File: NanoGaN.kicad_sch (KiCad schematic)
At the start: 9 parts, among them J1 U_DC, J2 GND, J3 Phase_U, J4 Phase_V, J5 Phase_W

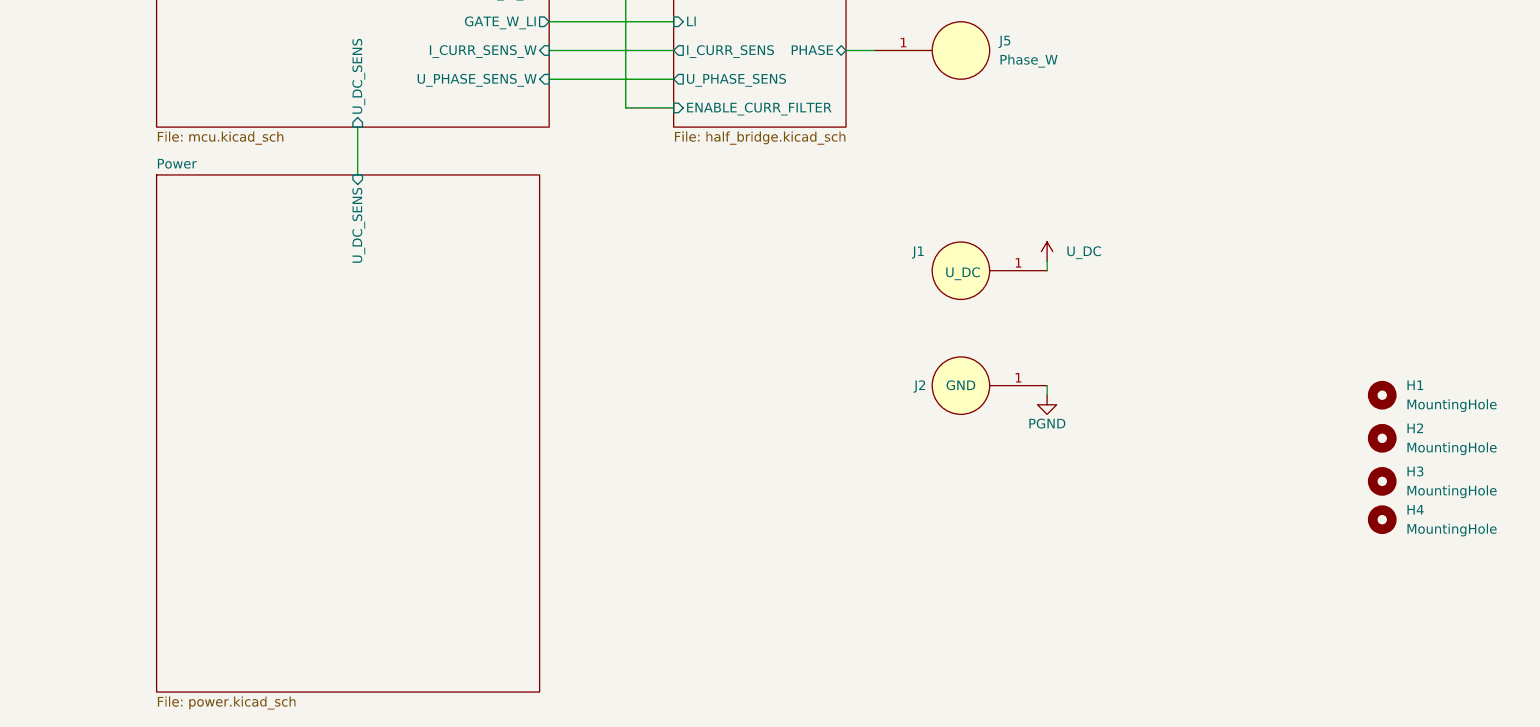
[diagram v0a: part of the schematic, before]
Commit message: Analog current filters were removed, some footprints were fixed and initial rough layout has been made.
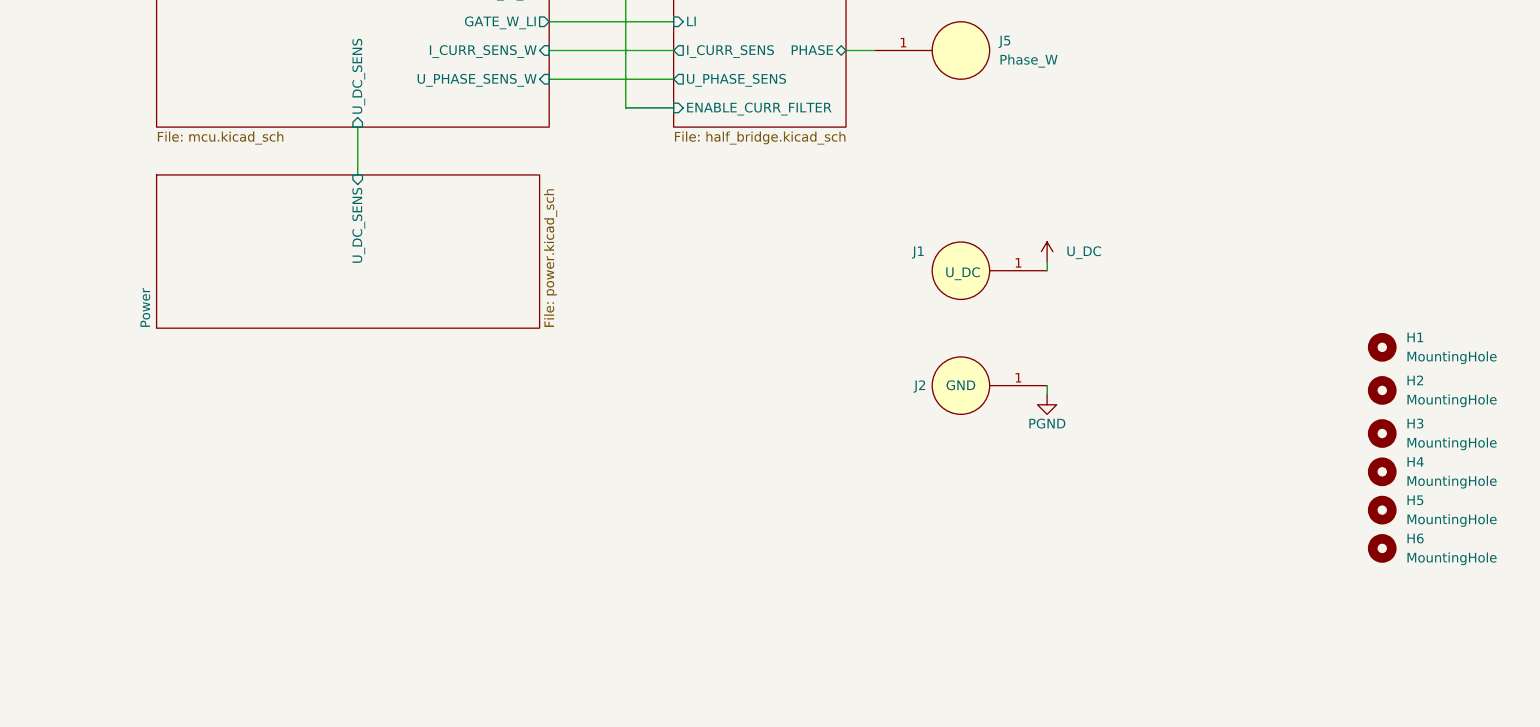
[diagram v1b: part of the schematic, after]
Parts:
- added H5, H6: MountingHole, MountingHole:MountingHole_3.2mm_M3, symbol Mechanical:MountingHole
- J1, J2, J3, J4, J5: footprint Connector:Power_Welding_Pad_10x10mm -> TerminalBlock_Wuerth:Wuerth_REDCUBE-THR_WP-THRBU_74650073_THR
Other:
- moved on the sheet: H1, H2, H3, H4
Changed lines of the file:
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@@
 			)
 		)
-		(property "Footprint" "Connector:Power_Welding_Pad_10x10mm"
+		(property "Footprint" "TerminalBlock_Wuerth:Wuerth_REDCUBE-THR_WP-THRBU_74650073_THR"
 			(at 205.74 93.98 0)
 			(effects
@@
 	)
 	(symbol
+		(lib_id "Mechanical:MountingHole")
+		(at 261.62 160.02 0)
+		(unit 1)
+		(exclude_from_sim no)
+		(in_bom yes)
+		(on_board yes)
+		(dnp no)
+		(fields_autoplaced yes)
+		(property "Reference" "H6"
+			(at 264.795 158.75 0)
+			(effects
+				(font
+					(size 1.27 1.27)
+				)
+				(justify left)
+			)
+		)
+		(property "Value" "MountingHole"
+			(at 264.795 161.29 0)
+			(effects
+				(font
+					(size 1.27 1.27)
+				)
+				(justify left)
+			)
+		)
+		(property "Footprint" "MountingHole:MountingHole_3.2mm_M3"
+			(at 261.62 160.02 0)
+			(effects
+				(font
+					(size 1.27 1.27)
+				)
+				(hide yes)
+			)
+		)
+		(property "Datasheet" "~"
+			(at 261.62 160.02 0)
+			(effects
+				(font
+					(size 1.27 1.27)
+				)
+				(hide yes)
+			)
+		)
+		(property "Description" ""
+			(at 261.62 160.02 0)
+			(effects
+				(font
+					(size 1.27 1.27)
+				)
+			)
+		)
+		(instances
+			(project "NanoGaN"
+				(path "/aa8a494f-605e-4a00-9d3c-daec94709fcb"
+					(reference "H6")
+					(unit 1)
+				)
+			)
+		)
+	)
+	(symbol
 		(lib_id "power:GND")
 		(at 217.17 139.7 0)
@@
 			)
 		)
-		(property "Footprint" "Connector:Power_Welding_Pad_10x10mm"
+		(property "Footprint" "TerminalBlock_Wuerth:Wuerth_REDCUBE-THR_WP-THRBU_74650073_THR"
 			(at 205.74 68.58 0)
 			(effects
@@
 			)
 		)
-		(property "Footprint" "Connector:Power_Welding_Pad_10x10mm"
+		(property "Footprint" "TerminalBlock_Wuerth:Wuerth_REDCUBE-THR_WP-THRBU_74650073_THR"
 			(at 205.74 123.19 0)
 			(effects
@@
 	(symbol
 		(lib_id "Mechanical:MountingHole")
-		(at 261.62 156.21 0)
+		(at 261.62 149.86 0)
 		(unit 1)
 		(exclude_from_sim no)
@@
 		(fields_autoplaced yes)
 		(property "Reference" "H4"
-			(at 264.795 154.94 0)
+			(at 264.795 148.59 0)
 			(effects
 				(font
@@
 		)
 		(property "Value" "MountingHole"
-			(at 264.795 157.48 0)
+			(at 264.795 151.13 0)
 			(effects
 				(font
@@
 		)
 		(property "Footprint" "MountingHole:MountingHole_3.2mm_M3"
-			(at 261.62 156.21 0)
+			(at 261.62 149.86 0)
 			(effects
 				(font
@@
 		)
 		(property "Datasheet" "~"
-			(at 261.62 156.21 0)
-			(effects
-				(font
-					(size 1.27 1.27)
-				)
-				(hide yes)
-			)
-		)
-		(property "Description" ""
-			(at 261.62 156.21 0)
+			(at 261.62 149.86 0)
+			(effects
+				(font
+					(size 1.27 1.27)
+				)
+				(hide yes)
+			)
+		)
+		(property "Description" ""
+			(at 261.62 149.86 0)
 			(effects
 				(font
@@
 				(path "/aa8a494f-605e-4a00-9d3c-daec94709fcb"
 					(reference "H4")
+					(unit 1)
+				)
+			)
+		)
+	)
+	(symbol
+		(lib_id "Mechanical:MountingHole")
+		(at 261.62 154.94 0)
+		(unit 1)
+		(exclude_from_sim no)
+		(in_bom yes)
+		(on_board yes)
+		(dnp no)
+		(fields_autoplaced yes)
+		(property "Reference" "H5"
+			(at 264.795 153.67 0)
+			(effects
+				(font
+					(size 1.27 1.27)
+				)
+				(justify left)
+			)
+		)
+		(property "Value" "MountingHole"
+			(at 264.795 156.21 0)
+			(effects
+				(font
+					(size 1.27 1.27)
+				)
+				(justify left)
+			)
+		)
+		(property "Footprint" "MountingHole:MountingHole_3.2mm_M3"
+			(at 261.62 154.94 0)
+			(effects
+				(font
+					(size 1.27 1.27)
+				)
+				(hide yes)
+			)
+		)
+		(property "Datasheet" "~"
+			(at 261.62 154.94 0)
+			(effects
+				(font
+					(size 1.27 1.27)
+				)
+				(hide yes)
+			)
+		)
+		(property "Description" ""
+			(at 261.62 154.94 0)
+			(effects
+				(font
+					(size 1.27 1.27)
+				)
+			)
+		)
+		(instances
+			(project "NanoGaN"
+				(path "/aa8a494f-605e-4a00-9d3c-daec94709fcb"
+					(reference "H5")
 					(unit 1)
 				)
@@
 			)
 		)
-		(property "Footprint" "Connector:Power_Welding_Pad_10x10mm"
+		(property "Footprint" "TerminalBlock_Wuerth:Wuerth_REDCUBE-THR_WP-THRBU_74650073_THR"
 			(at 205.74 138.43 0)
 			(effects
@@
 	(symbol
 		(lib_id "Mechanical:MountingHole")
-		(at 261.62 139.7 0)
+		(at 261.62 133.35 0)
 		(unit 1)
 		(exclude_from_sim no)
@@
 		(fields_autoplaced yes)
 		(property "Reference" "H1"
-			(at 264.795 138.43 0)
+			(at 264.795 132.08 0)
 			(effects
 				(font
@@
 		)
 		(property "Value" "MountingHole"
-			(at 264.795 140.97 0)
+			(at 264.795 134.62 0)
 			(effects
 				(font
@@
 		)
 		(property "Footprint" "MountingHole:MountingHole_3.2mm_M3"
-			(at 261.62 139.7 0)
+			(at 261.62 133.35 0)
 			(effects
 				(font
@@
 		)
 		(property "Datasheet" "~"
-			(at 261.62 139.7 0)
-			(effects
-				(font
-					(size 1.27 1.27)
-				)
-				(hide yes)
-			)
-		)
-		(property "Description" ""
-			(at 261.62 139.7 0)
+			(at 261.62 133.35 0)
+			(effects
+				(font
+					(size 1.27 1.27)
+				)
+				(hide yes)
+			)
+		)
+		(property "Description" ""
+			(at 261.62 133.35 0)
 			(effects
 				(font
@@
 			)
 		)
-		(property "Footprint" "Connector:Power_Welding_Pad_10x10mm"
+		(property "Footprint" "TerminalBlock_Wuerth:Wuerth_REDCUBE-THR_WP-THRBU_74650073_THR"
 			(at 205.74 43.18 0)
 			(effects
@@
 	(symbol
 		(lib_id "Mechanical:MountingHole")
-		(at 261.62 145.415 0)
+		(at 261.62 139.065 0)
 		(unit 1)
 		(exclude_from_sim no)
@@
 		(fields_autoplaced yes)
 		(property "Reference" "H2"
-			(at 264.795 144.145 0)
+			(at 264.795 137.795 0)
 			(effects
 				(font
@@
 		)
 		(property "Value" "MountingHole"
-			(at 264.795 146.685 0)
+			(at 264.795 140.335 0)
 			(effects
 				(font
@@
 		)
 		(property "Footprint" "MountingHole:MountingHole_3.2mm_M3"
-			(at 261.62 145.415 0)
+			(at 261.62 139.065 0)
 			(effects
 				(font
@@
 		)
 		(property "Datasheet" "~"
-			(at 261.62 145.415 0)
-			(effects
-				(font
-					(size 1.27 1.27)
-				)
-				(hide yes)
-			)
-		)
-		(property "Description" ""
-			(at 261.62 145.415 0)
+			(at 261.62 139.065 0)
+			(effects
+				(font
+					(size 1.27 1.27)
+				)
+				(hide yes)
+			)
+		)
+		(property "Description" ""
+			(at 261.62 139.065 0)
 			(effects
 				(font
@@
 	(symbol
 		(lib_id "Mechanical:MountingHole")
-		(at 261.62 151.13 0)
+		(at 261.62 144.78 0)
 		(unit 1)
 		(exclude_from_sim no)
@@
 		(fields_autoplaced yes)
 		(property "Reference" "H3"
-			(at 264.795 149.86 0)
+			(at 264.795 143.51 0)
 			(effects
 				(font
@@
 		)
 		(property "Value" "MountingHole"
-			(at 264.795 152.4 0)
+			(at 264.795 146.05 0)
 			(effects
 				(font
@@
 		)
 		(property "Footprint" "MountingHole:MountingHole_3.2mm_M3"
-			(at 261.62 151.13 0)
+			(at 261.62 144.78 0)
 			(effects
 				(font
@@
 		)
 		(property "Datasheet" "~"
-			(at 261.62 151.13 0)
-			(effects
-				(font
-					(size 1.27 1.27)
-				)
-				(hide yes)
-			)
-		)
-		(property "Description" ""
-			(at 261.62 151.13 0)
+			(at 261.62 144.78 0)
+			(effects
+				(font
+					(size 1.27 1.27)
+				)
+				(hide yes)
+			)
+		)
+		(property "Description" ""
+			(at 261.62 144.78 0)
 			(effects
 				(font
@@
 	(sheet
 		(at 99.06 110.49)
-		(size 50.8 68.58)
+		(size 50.8 20.32)
 		(exclude_from_sim no)
 		(in_bom yes)
@@
 		)
 		(property "Sheetname" "Power"
-			(at 99.06 109.7784 0)
+			(at 98.3484 130.81 90)
 			(effects
 				(font
@@
 		)
 		(property "Sheetfile" "power.kicad_sch"
-			(at 99.06 179.6546 0)
-			(effects
-				(font
+			(at 150.4446 130.81 90)
+			(effects
+				(font

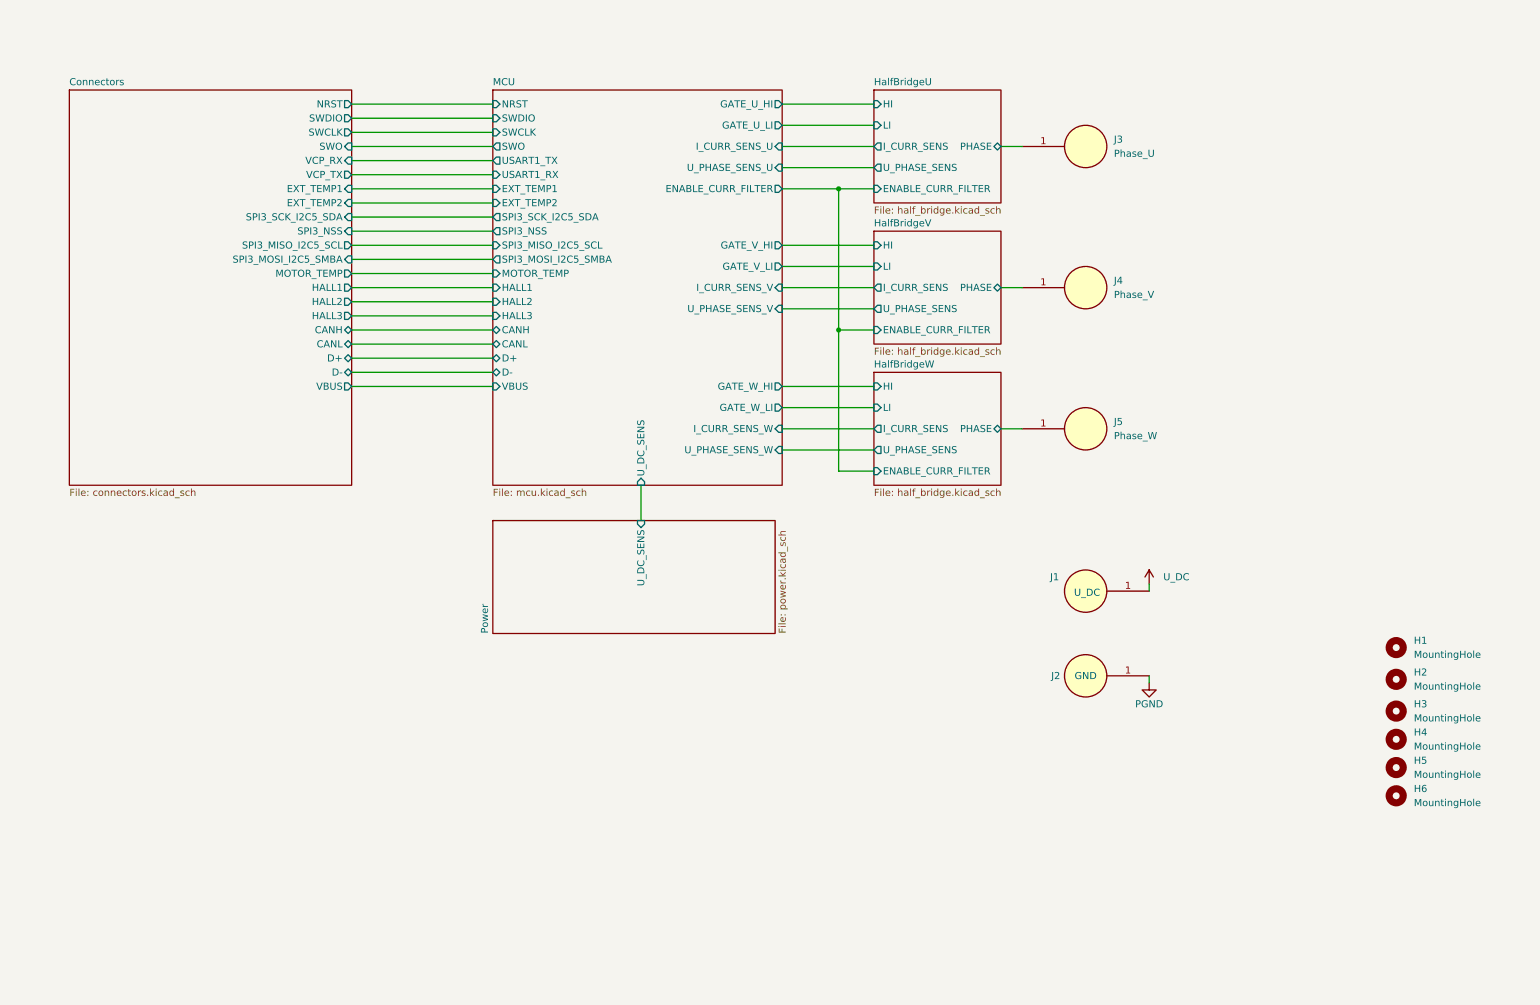
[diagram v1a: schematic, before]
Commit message: pdf export and small fixes
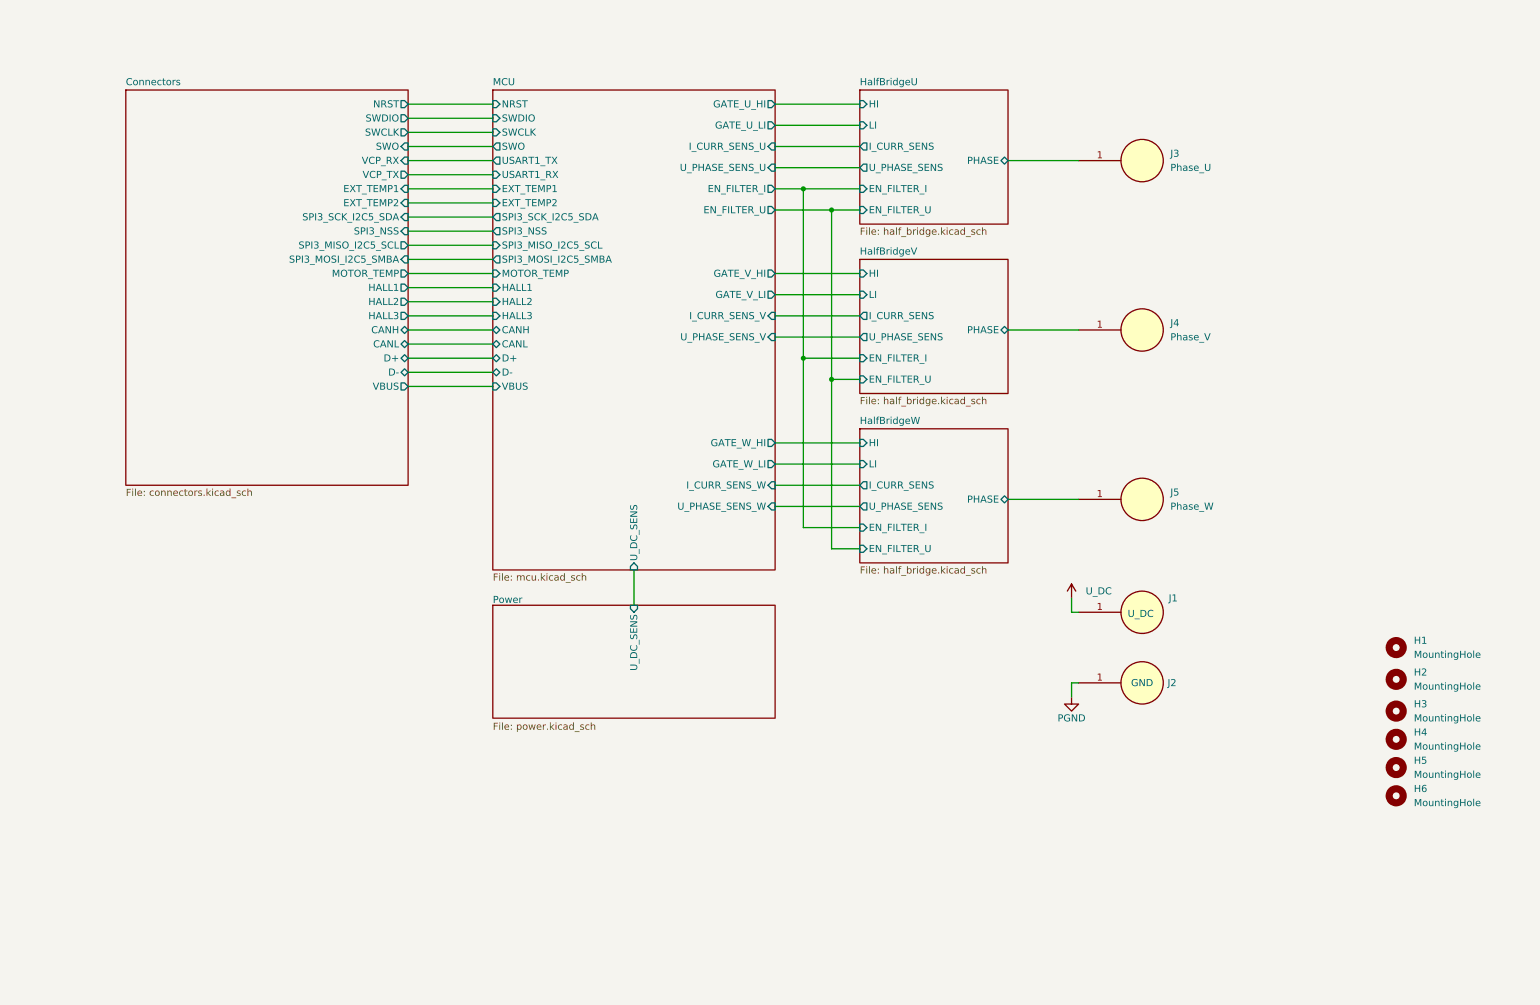
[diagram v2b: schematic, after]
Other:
- sheet HalfBridgeU ports: added EN_FILTER_I, EN_FILTER_U; removed ENABLE_CURR_FILTER
- sheet HalfBridgeV ports: added EN_FILTER_I, EN_FILTER_U; removed ENABLE_CURR_FILTER
- sheet HalfBridgeW ports: added EN_FILTER_I, EN_FILTER_U; removed ENABLE_CURR_FILTER
- sheet MCU ports: added EN_FILTER_I, EN_FILTER_U; removed ENABLE_CURR_FILTER
- moved on the sheet: J1, J2, J3, J4, J5

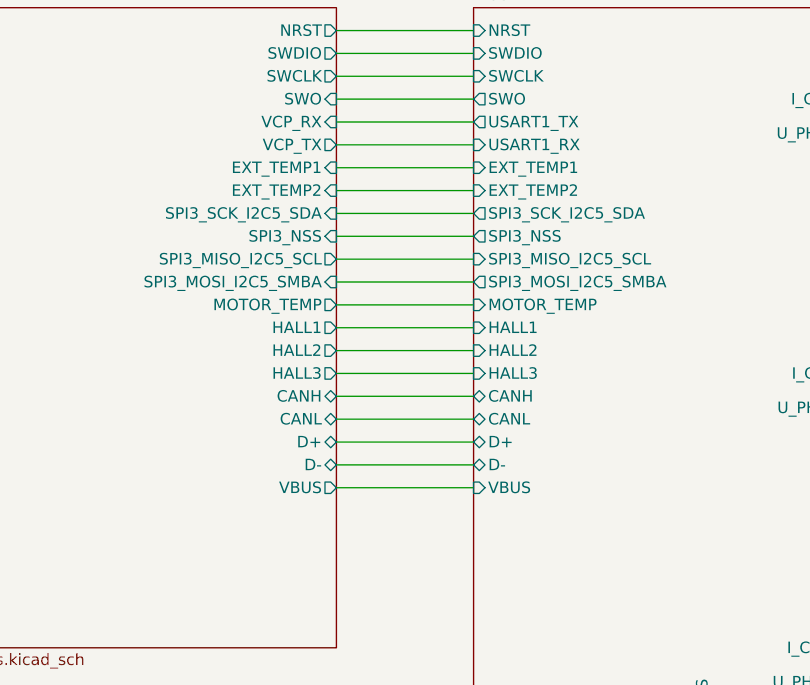
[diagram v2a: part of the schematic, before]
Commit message: Added PWM fan control
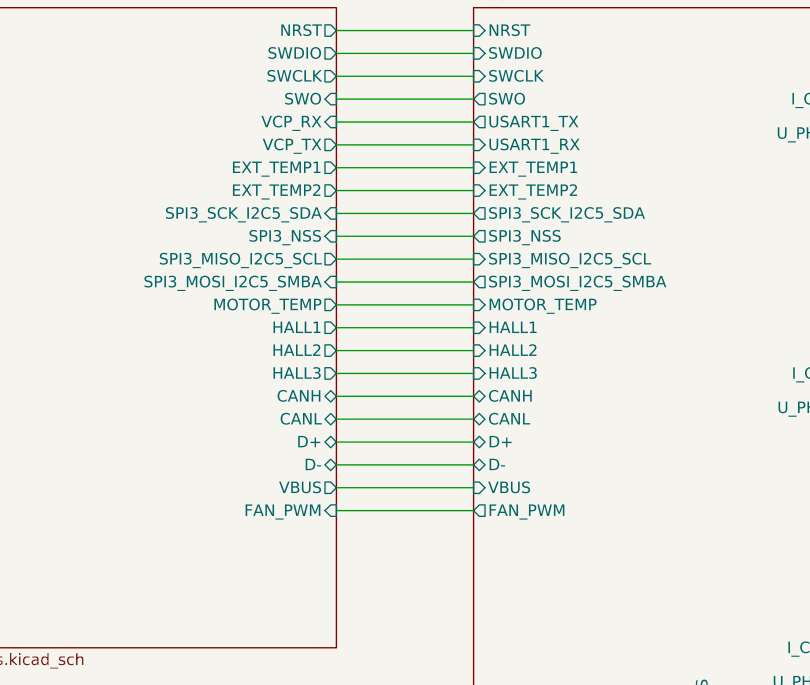
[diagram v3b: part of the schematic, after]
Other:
- sheet Connectors ports: added FAN_PWM; removed none
- sheet MCU ports: added FAN_PWM; removed none
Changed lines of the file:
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@@
+	(wire
+		(pts
+			(xy 83.82 88.9) (xy 99.06 88.9)
+		)
+		(stroke
+			(width 0)
+			(type default)
+		)
+	)
 	(wire
 		(pts
@@
 			)
 		)
-		(pin "EXT_TEMP1" input
-			(at 83.82 50.8 0)
-			(effects
-				(font
-					(size 1.27 1.27)
-				)
-				(justify right)
-			)
-		)
-		(pin "EXT_TEMP2" input
-			(at 83.82 53.34 0)
-			(effects
-				(font
-					(size 1.27 1.27)
-				)
-				(justify right)
-			)
-		)
 		(pin "SWO" input
 			(at 83.82 43.18 0)
@@
 		(pin "VBUS" output
 			(at 83.82 86.36 0)
+			(effects
+				(font
+					(size 1.27 1.27)
+				)
+				(justify right)
+			)
+		)
+		(pin "EXT_TEMP1" output
+			(at 83.82 50.8 0)
+			(effects
+				(font
+					(size 1.27 1.27)
+				)
+				(justify right)
+			)
+		)
+		(pin "EXT_TEMP2" output
+			(at 83.82 53.34 0)
+			(effects
+				(font
+					(size 1.27 1.27)
+				)
+				(justify right)
+			)
+		)
+		(pin "FAN_PWM" input
+			(at 83.82 88.9 0)
 			(effects
 				(font
@@
 			)
 		)
+		(pin "FAN_PWM" output
+			(at 99.06 88.9 180)
+			(effects
+				(font
+					(size 1.27 1.27)
+				)
+				(justify left)
+			)
+		)
